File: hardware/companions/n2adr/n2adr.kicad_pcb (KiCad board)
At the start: 4 copper layers, 100 x 50 mm, 162 parts, among them CN1 Audio-Jack-2, CN2 Conn_01x20, CN3 SMA, CN4 SMA, CN5 CONN_01X03, J3 Conn_01x01, K1 EC2-3NU, K2 EC2-3NU, K3 EC2-3NU, K4 EC2-3NU, K5 EC2-3NU, K6 EC2-3NU, K7 EC2-3NU, P1 TST, P13 TST, P14 TST, P15 TST, P16 TST, P2 TST, P3 TST, P4 TST, P5 TST, P6 TST, P7 TST, P8 TST, U1 MCP23008, U2 ULN2003LV, U3 AD8692, U5 74LVC1G00

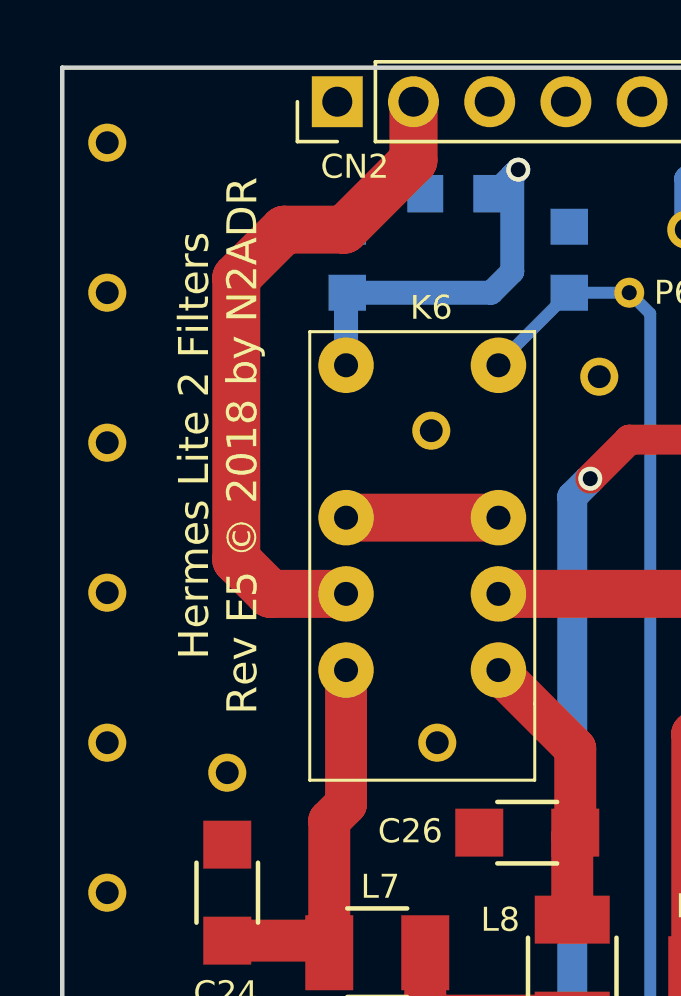
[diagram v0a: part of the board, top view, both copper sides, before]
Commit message: Updates to N2ADR filterboard for build8 group buy
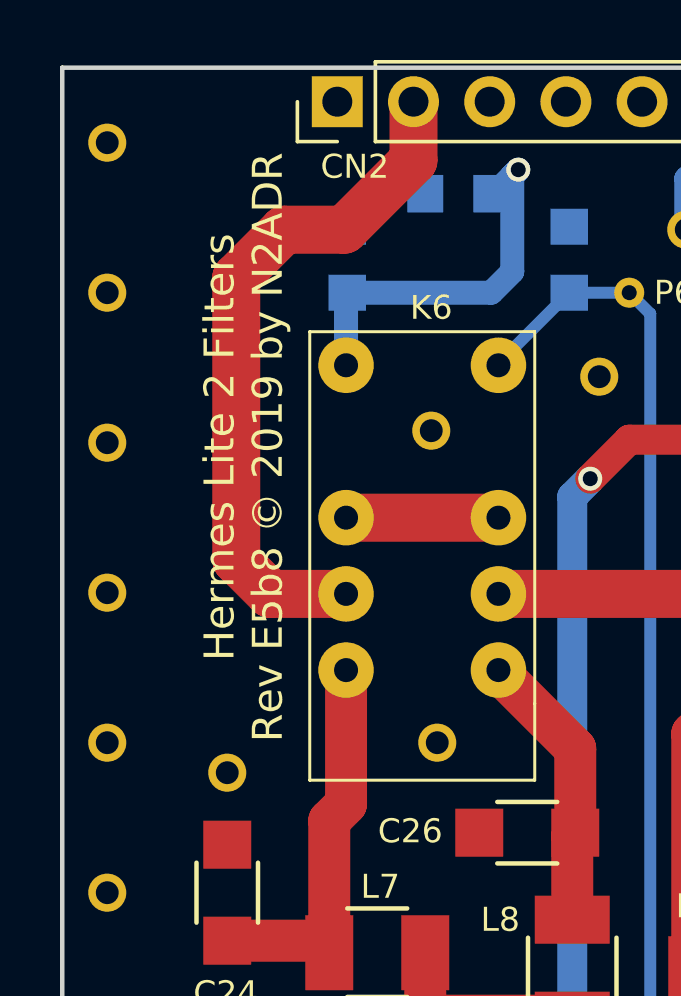
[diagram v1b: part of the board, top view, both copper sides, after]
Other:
- board text added: "Hermes Lite 2 Filters Rev E5b8 © 2019 by N2ADR"
- board text removed: "Hermes Lite 2 Filters Rev E5 © 2018 by N2ADR"
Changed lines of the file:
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@@
-(kicad_pcb (version 4) (host pcbnew 4.0.6)
+(kicad_pcb (version 20171130) (host pcbnew 5.0.2-bee76a0~70~ubuntu16.04.1)
   (general
-    (links 287)
-    (no_connects 0)
-    (area 62.5 52.295903 165.414286 115.34)
     (thickness 1.6)
     (drawings 17)
@@
   (title_block
     (title "HL2 Filter Board")
-    (date 2018-07-08)
-    (rev E5)
+    (date 2019-02-20)
+    (rev E5b8)
     (company N2ADR)
   )
@@
     (0 F.Cu signal)
     (1 In1.Cu signal)
-    (2 In2.Cu signal hide)
+    (2 In2.Cu signal)
     (31 B.Cu signal)
     (32 B.Adhes user)
@@
     (pad_drill 0.3302)
     (pad_to_mask_clearance 0.2)
+    (solder_mask_min_width 0.25)
     (aux_axis_origin 65 55)
     (visible_elements 7FFEFF7F)
     (pcbplotparams
-      (layerselection 0x010f0_80000007)
+      (layerselection 0x010fc_ffffffff)
       (usegerberextensions false)
+      (usegerberattributes false)
+      (usegerberadvancedattributes false)
+      (creategerberjobfile false)
       (excludeedgelayer true)
       (linewidth 0.100000)
@@
       (hpglpennumber 1)
       (hpglpenspeed 20)
-      (hpglpendiameter 15)
-      (hpglpenoverlay 2)
+      (hpglpendiameter 15.000000)
       (psnegative false)
       (psa4output false)
@@
       (drillshape 0)
       (scaleselection 1)
-      (outputdirectory gerber/))
+      (outputdirectory "gerber/"))
   )
   (net 0 "")
@@
   (module Local:RelayDPDT01 (layer F.Cu)
     (at 116 70 270)
-    (fp_text reference K3 (at -6.95 3.15 360) (layer F.SilkS)
+    (fp_text reference K3 (at -6.95 3.15) (layer F.SilkS)
       (effects (font (size 0.8 0.8) (thickness 0.1)))
     )
@@
   (module Local:RelayDPDT01 (layer F.Cu)
     (at 103 70 270)
-    (fp_text reference K4 (at -6.85 0.35 360) (layer F.SilkS)
+    (fp_text reference K4 (at -6.85 0.35) (layer F.SilkS)
       (effects (font (size 0.8 0.8) (thickness 0.1)))
     )
@@
     (tags "capacitor 0805")
     (attr smd)
-    (fp_text reference C1 (at 0.05 -1.8 540) (layer F.SilkS)
+    (fp_text reference C1 (at 0.05 -1.8 180) (layer F.SilkS)
       (effects (font (size 0.8 0.8) (thickness 0.1)))
     )
@@
     (tags "capacitor 0805")
     (attr smd)
-    (fp_text reference C2 (at -0.05 1.55 360) (layer F.SilkS)
+    (fp_text reference C2 (at -0.05 1.55) (layer F.SilkS)
       (effects (font (size 0.8 0.8) (thickness 0.1)))
     )
@@
     (tags "capacitor 0805")
     (attr smd)
-    (fp_text reference C3 (at -2.5 -0.2 360) (layer B.SilkS)
+    (fp_text reference C3 (at -2.5 -0.2) (layer B.SilkS)
       (effects (font (size 0.8 0.8) (thickness 0.1)) (justify mirror))
     )
@@
     (tags "capacitor 0805")
     (attr smd)
-    (fp_text reference C5 (at -2.55 -1.35 540) (layer B.SilkS)
+    (fp_text reference C5 (at -2.55 -1.35 180) (layer B.SilkS)
       (effects (font (size 0.8 0.8) (thickness 0.1)) (justify mirror))
     )
@@
     (tags "capacitor 0805")
     (attr smd)
-    (fp_text reference C6 (at -2.55 -0.05 360) (layer B.SilkS)
+    (fp_text reference C6 (at -2.55 -0.05) (layer B.SilkS)
       (effects (font (size 0.8 0.8) (thickness 0.1)) (justify mirror))
     )
@@
     (tags "capacitor 0805")
     (attr smd)
-    (fp_text reference C14 (at -1.1 -2.25 360) (layer B.SilkS)
+    (fp_text reference C14 (at -1.1 -2.25) (layer B.SilkS)
       (effects (font (size 0.8 0.8) (thickness 0.1)) (justify mirror))
     )
@@
     (tags "capacitor 0805")
     (attr smd)
-    (fp_text reference R5 (at -2.25 -1.85 360) (layer B.SilkS)
+    (fp_text reference R5 (at -2.25 -1.85) (layer B.SilkS)
       (effects (font (size 0.8 0.8) (thickness 0.1)) (justify mirror))
     )
@@
     (tags "capacitor 0805")
     (attr smd)
-    (fp_text reference R8 (at -2.8 -0.3 360) (layer B.SilkS)
+    (fp_text reference R8 (at -2.8 -0.3) (layer B.SilkS)
       (effects (font (size 0.8 0.8) (thickness 0.1)) (justify mirror))
     )
@@
     (tags "capacitor 1206")
     (attr smd)
-    (fp_text reference C22 (at -0.1 1.85 450) (layer F.SilkS)
+    (fp_text reference C22 (at -0.1 1.85 90) (layer F.SilkS)
       (effects (font (size 0.8 0.8) (thickness 0.1)))
     )
@@
     (tags "capacitor 1206")
     (attr smd)
-    (fp_text reference C24 (at 3.35 0.05 360) (layer F.SilkS)
+    (fp_text reference C24 (at 3.35 0.05) (layer F.SilkS)
       (effects (font (size 0.8 0.8) (thickness 0.1)))
     )
@@
     (tags "capacitor 1210")
     (attr smd)
-    (fp_text reference L8 (at 1.6 -2.4 360) (layer F.SilkS)
+    (fp_text reference L8 (at 1.6 -2.4) (layer F.SilkS)
       (effects (font (size 0.8 0.8) (thickness 0.1)))
     )
@@
     (tags "capacitor 0805")
     (attr smd)
-    (fp_text reference C27 (at -2.55 0.2 540) (layer B.SilkS)
+    (fp_text reference C27 (at -2.55 0.2 180) (layer B.SilkS)
       (effects (font (size 0.8 0.8) (thickness 0.1)) (justify mirror))
     )
@@
     (tags "capacitor 0805")
     (attr smd)
-    (fp_text reference C28 (at -2.65 -0.6 540) (layer B.SilkS)
+    (fp_text reference C28 (at -2.65 -0.6 180) (layer B.SilkS)
       (effects (font (size 0.8 0.8) (thickness 0.1)) (justify mirror))
     )
@@
     (tags "capacitor 0805")
     (attr smd)
-    (fp_text reference C29 (at -2.9 -0.1 360) (layer B.SilkS)
+    (fp_text reference C29 (at -2.9 -0.1) (layer B.SilkS)
       (effects (font (size 0.8 0.8) (thickness 0.1)) (justify mirror))
     )
@@
     (tags "capacitor 0805")
     (attr smd)
-    (fp_text reference C30 (at -3.25 -0.2 360) (layer B.SilkS)
+    (fp_text reference C30 (at -3.25 -0.2) (layer B.SilkS)
       (effects (font (size 0.8 0.8) (thickness 0.1)) (justify mirror))
     )
@@
     (tags "capacitor 0805")
     (attr smd)
-    (fp_text reference C31 (at -0.1 -2 360) (layer B.SilkS)
+    (fp_text reference C31 (at -0.1 -2) (layer B.SilkS)
       (effects (font (size 0.8 0.8) (thickness 0.1)) (justify mirror))
     )
@@
     (tags "capacitor 0805")
     (attr smd)
-    (fp_text reference C20 (at -0.1 2.2 540) (layer B.SilkS)
+    (fp_text reference C20 (at -0.1 2.2 180) (layer B.SilkS)
       (effects (font (size 0.8 0.8) (thickness 0.1)) (justify mirror))
     )
@@
     (tags "capacitor 0805")
     (attr smd)
-    (fp_text reference R4 (at -2.1 2.05 360) (layer B.SilkS)
+    (fp_text reference R4 (at -2.1 2.05) (layer B.SilkS)
       (effects (font (size 0.8 0.8) (thickness 0.1)) (justify mirror))
     )
@@
     (tags "SSOP 0.65")
     (attr smd)
-    (fp_text reference U3 (at -0.3 -2.85 540) (layer B.SilkS)
+    (fp_text reference U3 (at -0.3 -2.85 180) (layer B.SilkS)
       (effects (font (size 0.8 0.8) (thickness 0.1)) (justify mirror))
     )
@@
     (tags "capacitor 0805")
     (attr smd)
-    (fp_text reference C50 (at 1.6 -2.1 360) (layer F.SilkS)
+    (fp_text reference C50 (at 1.6 -2.1) (layer F.SilkS)
       (effects (font (size 0.8 0.8) (thickness 0.1)))
     )
@@
     (tags "capacitor 0805")
     (attr smd)
-    (fp_text reference C49 (at 0.1 1.5 450) (layer F.SilkS)
+    (fp_text reference C49 (at 0.1 1.5 90) (layer F.SilkS)
       (effects (font (size 0.8 0.8) (thickness 0.1)))
     )
@@
   (module Local:RelayDPDT01 (layer F.Cu)
     (at 129 68 270)
-    (fp_text reference K2 (at -6.9 3 360) (layer F.SilkS)
+    (fp_text reference K2 (at -6.9 3) (layer F.SilkS)
       (effects (font (size 0.8 0.8) (thickness 0.1)))
     )
@@
   (module Local:RelayDPDT01 (layer F.Cu)
     (at 90 70 270)
-    (fp_text reference K5 (at -6.9 -0.2 360) (layer F.SilkS)
+    (fp_text reference K5 (at -6.9 -0.2) (layer F.SilkS)
       (effects (font (size 0.8 0.8) (thickness 0.1)))
     )
@@
   (module Local:RelayDPDT01 (layer F.Cu)
     (at 77 70 270)
-    (fp_text reference K6 (at -7 -0.3 360) (layer F.SilkS)
+    (fp_text reference K6 (at -7 -0.3) (layer F.SilkS)
       (effects (font (size 0.8 0.8) (thickness 0.1)))
     )
@@
       (net 1 GND))
     (model Pin_Headers.3dshapes/Pin_Header_Straight_1x03.wrl
-      (at (xyz 0 -0.1 0))
+      (offset (xyz 0 -2.539999961853027 0))
       (scale (xyz 1 1 1))
       (rotate (xyz 0 0 90))
@@
       (effects (font (size 0.8 0.8) (thickness 0.1)) (justify mirror))
     )
-    (fp_text user %R (at 0 0 360) (layer B.Fab)
+    (fp_text user %R (at 0 0) (layer B.Fab)
       (effects (font (size 0.8 0.8) (thickness 0.1)) (justify mirror))
     )
@@
     )
   )
-  (target plus (at 65 55) (size 5) (width 0.15) (layer Edge.Cuts))
+  (gr_text "Hermes Lite 2 Filters\nRev E5b8 © 2019 by N2ADR" (at 158.1 69.25 90) (layer B.SilkS)
+    (effects (font (size 1 1) (thickness 0.2)) (justify mirror))
+  )
   (gr_line (start 135 105) (end 165 105) (angle 90) (layer Edge.Cuts) (width 0.15))
   (gr_line (start 103 105) (end 123 105) (angle 90) (layer Edge.Cuts) (width 0.15))
@@
   (gr_circle (center 114.4 102.4) (end 114.2 102.8) (layer B.SilkS) (width 0.2))
   (gr_circle (center 126.1 89.5) (end 125.8 89.7) (layer B.SilkS) (width 0.2))
-  (gr_text "Hermes Lite 2 Filters\nRev E5 © 2018 by N2ADR" (at 70.2 67.6 90) (layer F.SilkS)
+  (gr_text "Hermes Lite 2 Filters\nRev E5b8 © 2019 by N2ADR" (at 71.05 67.65 90) (layer F.SilkS)
     (effects (font (size 1 1) (thickness 0.2)))
   )

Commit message: N2ADR work
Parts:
- added G***: OSHW-logo_silkscreen-front_2mm, N2ADR:OSHW-logo_silkscreen-front_2mm, F.Cu at (69.7, 57.7)
- added G***: OSHW-logo_silkscreen-back_2mm, N2ADR:OSHW-logo_silkscreen-back_2mm, B.Cu at (156.7, 59.7)
- added REF**: via, Local:via30, F.Cu at (146.9, 80.0)
- added REF**: via, Local:via30, F.Cu at (122.1, 70.0)
- moved REF** 4.11 mm to (148.3, 72.5)
- moved CN1 0.10 mm to (77.0, 103.4)
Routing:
- net Band7: track 54.8 -> 58.3 mm
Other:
- board size 100 x 50 mm -> 100 x 49.9 mm
- board text added: "Hermes Lite 2 Filters Rev E5b9 © 2019 by N2ADR"
- board text removed: "Hermes Lite 2 Filters Rev E5b8 © 2019 by N2ADR"
